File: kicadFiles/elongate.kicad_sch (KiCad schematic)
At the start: 137 parts, among them J1 TYPE-C-31-M12_13, SW1 MXSwitch, SW10 MXSwitch, SW11 MXSwitch, SW12 MXSwitch, SW13 MXSwitch, SW14 MXSwitch, SW15 MXSwitch, SW16 MXSwitch, SW17 MXSwitch, SW18 MXSwitch, SW19 MXSwitch, SW2 MXSwitch, SW20 MXSwitch, SW21 MXSwitch, SW22 MXSwitch, SW23 MXSwitch, SW24 MXSwitch, SW25 MXSwitch, SW26 MXSwitch, SW27 MXSwitch, SW28 MXSwitch, SW29 MXSwitch, SW3 MXSwitch, SW30 MXSwitch, SW31 MXSwitch, SW32 MXSwitch, SW33 MXSwitch, SW34 MXSwitch, SW35 MXSwitch, SW36 MXSwitch, SW37 MXSwitch, SW38 MXSwitch, SW39 MXSwitch, SW4 MXSwitch, SW40 MXSwitch, SW41 MXSwitch, SW42 MXSwitch, SW43 MXSwitch, SW44 MXSwitch, SW45 MXSwitch, SW46 MXSwitch, SW47 MXSwitch, SW48 MXSwitch, SW49 MXSwitch, SW5 MXSwitch, SW50 MXSwitch, SW51 MXSwitch, SW52 MXSwitch, SW53 MXSwitch, SW54 MXSwitch, SW6 MXSwitch, SW7 MXSwitch, SW8 MXSwitch, SW9 MXSwitch, U1 TPD4E05U06DQAR

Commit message: Change RCC resistors to R0402
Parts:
- R2, R3: footprint Resistor_SMD:R_0805_2012Metric_Pad1.15x1.40mm_HandSolder -> Resistor_SMD:R_0402_1005Metric; Package R1206 -> R0402

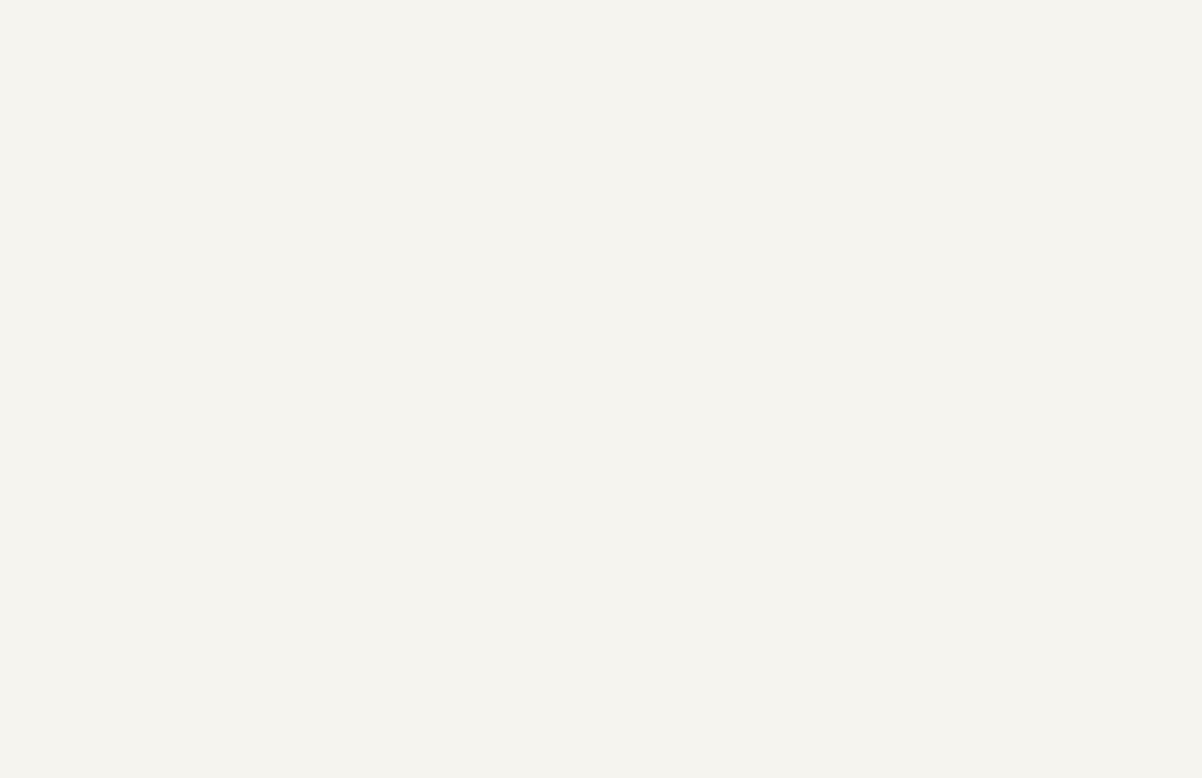
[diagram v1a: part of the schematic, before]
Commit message: Added LEDs
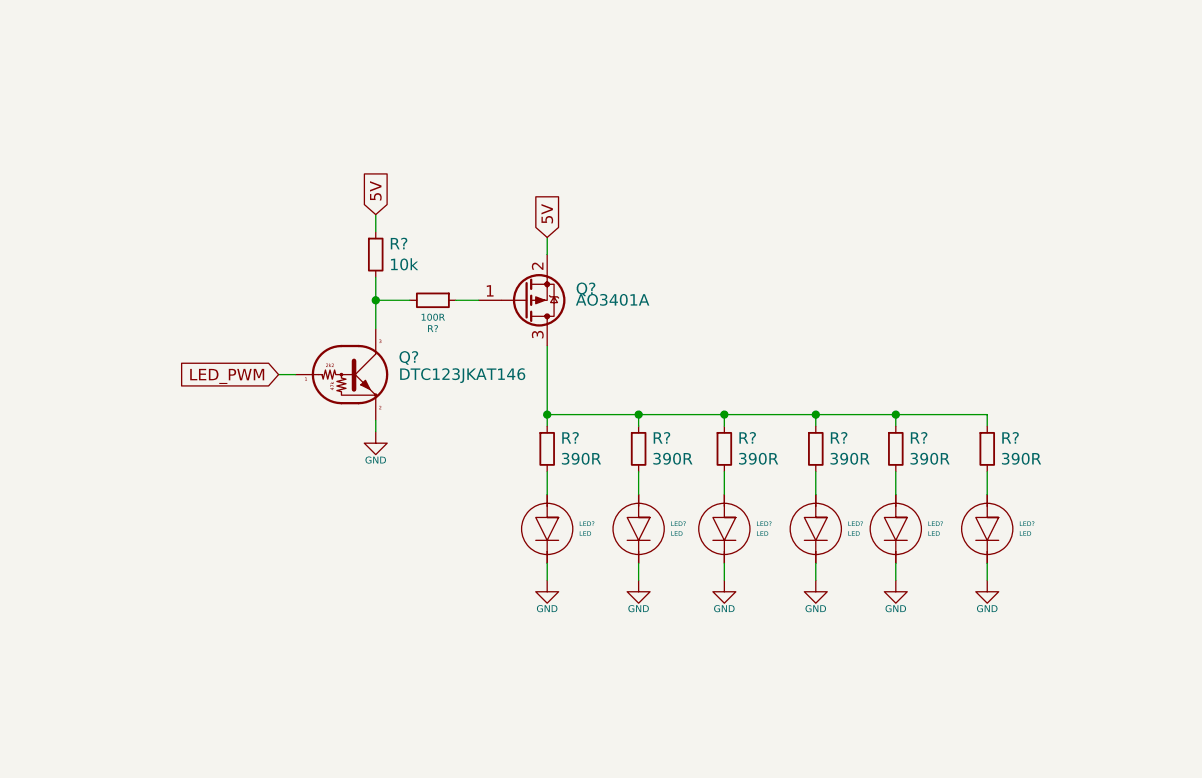
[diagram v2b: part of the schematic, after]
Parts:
- added LED? (x6): LED, acheron_Components:LED_THT_2.54mm, symbol acheronSymbols:LED
- added Q?: DTC123JKAT146, Package_TO_SOT_SMD:SOT-23, symbol acheronSymbols:DTC123J
- added Q?: AO3401A, Package_TO_SOT_SMD:SOT-23, symbol Transistor_FET:AO3401A
- added R? (x6): 390R, acheron_Components:R_SMD_1206, symbol Device:R_Small
- added R?: 100R, acheron_Components:R_SMD_1206, symbol Device:R_Small
- added R?: 10k, acheron_Components:R_SMD_1206, symbol Device:R_Small
- R10, R5, R6, R7, R8, R9: Package (none) -> R1206
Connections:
- net 5V: now also Q?.2 (S), R?.1
- net GND: now also LED?.K, LED?.K, LED?.K, LED?.K, LED?.K, LED?.K, Q?.2 (E)
- new net: Q?.3 (D), R?.1, R?.1, R?.1, R?.1, R?.1, R?.1
- new net: LED?.A, R?.2 (x6)
- new net: Q?.1 (G), R?.1
- new net: Q?.3 (C), R?.2, R?.2
- new net LED_PWM: Q?.1 (B)

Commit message: Finish LED placin, add MCU
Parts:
- added J2: AVR-JTAG-10, acheron_Connectors:Conn_ARM_JTAG_SWD_10, symbol Connector:AVR-JTAG-10
- added LED13, LED14, LED15, LED16, LED17, LED18, LED19, LED20, LED21, LED22, LED23, LED24, LED25, LED26, LED27, LED28, LED29, LED30, LED31, LED32, LED33, LED34, LED35, LED36, LED37, LED38, LED39, LED40, LED41, LED42, LED43, LED44, LED45, LED46, LED47, LED48, LED49, LED50, LED51, LED52, LED53, LED54, LED55, LED56, LED57, LED58, LED59, LED60: LED, acheron_Components:LED_THT_2.54mm, symbol acheronSymbols:LED
- added R20, R21, R22, R23, R24, R25, R26, R27, R28, R29, R30, R31, R32, R33, R34, R35, R36, R37, R38, R39, R40, R41, R42, R43, R44, R45, R46, R47, R48, R49, R50, R51, R52, R53, R54, R55, R56, R57, R58, R59, R60, R61, R62, R63, R64, R65, R66, R67: 390R, acheron_Components:R_SMD_1206, symbol Device:R_Small
- added U2: STM32F072CBT6, acheron_Components:LQFP-48_7x7mm_P0.5mm, symbol acheronSymbols:STM32F072-LQFP48
- gave numbers to parts that had none: 16
- renumbered C2 to C1, C1 to C2, D16 to D14, D17 to D15, D18 to D16, D19 to D17, D20 to D18, D21 to D19, D22 to D20, D23 to D21, D24 to D22, D25 to D23, D26 to D24, D27 to D25, D30 to D26, D31 to D27, D32 to D28, D33 to D29, D34 to D30, D35 to D31, D36 to D32, D37 to D33, D38 to D34, D39 to D35, D40 to D36, D41 to D37, D44 to D38, D45 to D39, D46 to D40, D47 to D41, D48 to D42, D49 to D43, D50 to D44, D51 to D45, D52 to D46, D42 to D47, D53 to D48, D15 to D49, D29 to D50, D43 to D51, D54 to D52, D14 to D53, D28 to D54, R2 to R1, R3 to R2, R4 to R3, R1 to R4, SW16 to SW14, SW17 to SW15, SW18 to SW16, SW19 to SW17, SW20 to SW18, SW21 to SW19, SW22 to SW20, SW23 to SW21, SW24 to SW22, SW25 to SW23, SW26 to SW24, SW27 to SW25, SW30 to SW26, SW31 to SW27, SW32 to SW28, SW33 to SW29, SW34 to SW30, SW35 to SW31, SW36 to SW32, SW37 to SW33, SW38 to SW34, SW39 to SW35, SW40 to SW36, SW41 to SW37, SW44 to SW38, SW45 to SW39, SW46 to SW40, SW47 to SW41, SW48 to SW42, SW49 to SW43, SW50 to SW44, SW51 to SW45, SW52 to SW46, SW42 to SW47, SW53 to SW48, SW15 to SW49, SW29 to SW50, SW43 to SW51, SW54 to SW52, SW14 to SW53, SW28 to SW54
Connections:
- net Col10: no longer SW53.1 (Col)
- net Col11: no longer SW54.1 (Col)
- net Col12: no longer SW47.1 (Col)
- net Col13: no longer SW48.1 (Col)
- net Col2: no longer SW49.1 (Col)
- net Col3: no longer SW50.1 (Col)
- net Col5: no longer SW51.1 (Col)
- net Col8: no longer SW52.1 (Col)
- net D+: now also U2.33 (USB_DP/PA12)
- net D-: now also U2.32 (USB_DM/TIM1_CH4/PA11)
- net GND: now also LED13.K, LED14.K, LED15.K, LED16.K, LED17.K, LED18.K, LED19.K, LED20.K, LED21.K, LED22.K, LED23.K, LED24.K, LED25.K, LED26.K, LED27.K, LED28.K, LED29.K, LED30.K, LED31.K, LED32.K, LED33.K, LED34.K, LED35.K, LED36.K, LED37.K, LED38.K, LED39.K, LED40.K, LED41.K, LED42.K, LED43.K, LED44.K, LED45.K, LED46.K, LED47.K, LED48.K, LED49.K, LED50.K, LED51.K, LED52.K, LED53.K, LED54.K, LED55.K, LED56.K, LED57.K, LED58.K, LED59.K, LED60.K
- net LED_PWM: now also U2.16 (PA6/ADC_IN6/TIM3_CH1/TIM16_CH1)
- net Row1: now also D49.1 (K), D53.1 (K)
- net Row2: now also D50.1 (K), D54.1 (K)
- net Row3: now also D47.1 (K), D51.1 (K)
- net Row4: now also D48.1 (K), D52.1 (K)
- net at Q1.3 (D), R14.1, R15.1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: now also R20.1, R21.1, R22.1, R23.1, R24.1, R25.1, R26.1, R27.1, R28.1, R29.1, R30.1, R31.1, R32.1, R33.1, R34.1, R35.1, R36.1, R37.1, R38.1, R39.1, R40.1, R41.1, R42.1, R43.1, R44.1, R45.1, R46.1, R47.1, R48.1, R49.1, R50.1, R51.1, R52.1, R53.1, R54.1, R55.1, R56.1, R57.1, R58.1, R59.1, R60.1, R61.1, R62.1, R63.1, R64.1, R65.1, R66.1, R67.1
- removed net Row5: D47.1 (K), D48.1 (K), D49.1 (K), D50.1 (K), D51.1 (K), D52.1 (K), D53.1 (K), D54.1 (K)
- new net: LED50.A, R57.2
- new net: LED47.A, R54.2
- new net: LED24.A, R31.2
- new net: LED60.A, R67.2
- new net: LED57.A, R64.2
- new net: LED30.A, R37.2
- new net: LED41.A, R48.2
- new net: LED32.A, R39.2
- new net: LED14.A, R21.2
- new net: LED36.A, R43.2
- new net: LED35.A, R42.2
- new net: LED23.A, R30.2
- new net: LED31.A, R38.2
- new net: LED48.A, R55.2
- new net: LED53.A, R60.2
- new net: LED56.A, R63.2
- new net: LED25.A, R32.2
- new net: LED45.A, R52.2
- new net: LED51.A, R58.2
- new net: LED44.A, R51.2
- new net: LED17.A, R24.2
- new net: LED16.A, R23.2
- new net: LED34.A, R41.2
- new net: LED18.A, R25.2
- new net: LED21.A, R28.2
- new net: LED39.A, R46.2
- new net: LED46.A, R53.2
- new net: LED19.A, R26.2
- new net: LED42.A, R49.2
- new net: LED29.A, R36.2
- new net: J2.10 (GND), J2.2 (GND)
- new net: LED26.A, R33.2
- new net: LED33.A, R40.2
- new net: LED49.A, R56.2
- new net: LED15.A, R22.2
- new net: LED22.A, R29.2
- new net: LED55.A, R62.2
- new net: LED20.A, R27.2
- new net: LED58.A, R65.2
- new net: LED37.A, R44.2
- new net: LED38.A, R45.2
- new net: LED59.A, R66.2
- new net: LED54.A, R61.2
- new net: LED52.A, R59.2
- new net: LED43.A, R50.2
- new net: LED27.A, R34.2
- new net: LED13.A, R20.2
- new net: LED28.A, R35.2
- new net: LED40.A, R47.2
- new net Col14: SW47.1 (Col), SW48.1 (Col), SW53.1 (Col), SW54.1 (Col)
- new net Col15: SW49.1 (Col), SW50.1 (Col), SW51.1 (Col), SW52.1 (Col)
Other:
- moved on the sheet: C3, D47, D48, D49, D50, D51, D52, D53, D54, D55, F1, LED10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

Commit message: Almost finish routing, DRC pending
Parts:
- removed J2: AVR-JTAG-10, acheron_Connectors:Conn_ARM_JTAG_SWD_10, symbol Connector:AVR-JTAG-10
- added C10, C11, C12, C13, C14, C15, C16, C17, C18, C19, C4, C5, C6, C7, C8, C9: 1u, Capacitor_SMD:C_0805_2012Metric_Pad1.15x1.40mm_HandSolder, symbol Device:C_Small
- added C20: 100u, Capacitor_SMD:C_0805_2012Metric_Pad1.15x1.40mm_HandSolder, symbol Device:C_Small
- added C21: 10u, Capacitor_SMD:C_0805_2012Metric_Pad1.15x1.40mm_HandSolder, symbol Device:C_Small
- added D56, D57, D58, D59, D60, D61, D62, D63, D64, D65, D66, D67, D68, D69, D70, D71: WS2812C, acheron_Components:LED_WS2812B_5.0x5.0mm_P3.2mm, symbol LED:WS2812B
- added D72: 1N4148, acheron_Components:D_SOD-123, symbol Device:D
- added J2: Conn_ARM_JTAG_SWD_10, acheron_Connectors:Conn_ARM_JTAG_SWD_10, symbol Connector:Conn_ARM_JTAG_SWD_10
- added J3: Conn_01x11, acheron_Connectors:PinHeader_2x5_P2.54mm_Vertical, symbol Connector_Generic:Conn_01x11
- added Q3: AO3401A, Package_TO_SOT_SMD:SOT-23, symbol Transistor_FET:AO3401A
- added Q4: DTC123JKAT146, Package_TO_SOT_SMD:SOT-23, symbol acheronSymbols:DTC123J
- added R68, R69, R70, R71, R72, R73, R74, R75, R76, R77, R78, R79, R80, R81, R82, R83: 3R, acheron_Components:R_SMD_1206, symbol Device:R_Small
- added R84, R86: 10k, acheron_Components:R_SMD_1206, symbol Device:R_Small
- added R85: 5.1k, acheron_Components:R_SMD_1206, symbol Device:R_Small
- added R87: 100k, acheron_Components:R_SMD_1206, symbol Device:R_Small
- added R88: 100R, acheron_Components:R_SMD_1206, symbol Device:R_Small
- added R89: 33k, acheron_Components:R_SMD_1206, symbol Device:R_Small
- added SW55: SW_Push, acheron_Hardware:smdPushBtn, symbol Switch:SW_Push
- D1, D10, D11, D12, D13, D2, D3, D4, D5, D6, D7, D8, D9: Package (none) -> SOD-123
- D14: renamed from D53; Package (none) -> SOD-123
- D15: renamed from D49; Package (none) -> SOD-123
- D16: renamed from D14; Package (none) -> SOD-123
- D17: renamed from D15; Package (none) -> SOD-123
- D18: renamed from D16; Package (none) -> SOD-123
- D19: renamed from D17; Package (none) -> SOD-123
- D20: renamed from D18; Package (none) -> SOD-123
- D21: renamed from D19; Package (none) -> SOD-123
- D22: renamed from D20; Package (none) -> SOD-123
- D23: renamed from D21; Package (none) -> SOD-123
- D24: renamed from D22; Package (none) -> SOD-123
- D25: renamed from D23; Package (none) -> SOD-123
- D26: renamed from D24; Package (none) -> SOD-123
- D27: renamed from D25; Package (none) -> SOD-123
- D28: renamed from D54; Package (none) -> SOD-123
- D29: renamed from D50; Package (none) -> SOD-123
- D30: renamed from D26; Package (none) -> SOD-123
- D31: renamed from D27; Package (none) -> SOD-123
- D32: renamed from D28; Package (none) -> SOD-123
- D33: renamed from D29; Package (none) -> SOD-123
- D34: renamed from D30; Package (none) -> SOD-123
- D35: renamed from D31; Package (none) -> SOD-123
- D36: renamed from D32; Package (none) -> SOD-123
- D37: renamed from D33; Package (none) -> SOD-123
- D38: renamed from D34; Package (none) -> SOD-123
- D39: renamed from D35; Package (none) -> SOD-123
- D40: renamed from D36; Package (none) -> SOD-123
- D41: renamed from D37; Package (none) -> SOD-123
- D42: renamed from D47; Package (none) -> SOD-123
- D43: renamed from D51; Package (none) -> SOD-123
- D44: renamed from D38; Package (none) -> SOD-123
- D45: renamed from D39; Package (none) -> SOD-123
- D46: renamed from D40; Package (none) -> SOD-123
- D47: renamed from D41; Package (none) -> SOD-123
- D48: renamed from D42; Package (none) -> SOD-123
- D49: renamed from D43; Package (none) -> SOD-123
- D50: renamed from D44; Package (none) -> SOD-123
- D51: renamed from D45; Package (none) -> SOD-123
- D52: renamed from D46; Package (none) -> SOD-123
- D53: renamed from D48; Package (none) -> SOD-123
- D54: renamed from D52; Package (none) -> SOD-123
- renumbered SW53 to SW14, SW49 to SW15, SW14 to SW16, SW15 to SW17, SW16 to SW18, SW17 to SW19, SW18 to SW20, SW19 to SW21, SW20 to SW22, SW21 to SW23, SW22 to SW24, SW23 to SW25, SW24 to SW26, SW25 to SW27, SW54 to SW28, SW50 to SW29, SW26 to SW30, SW27 to SW31, SW28 to SW32, SW29 to SW33, SW30 to SW34, SW31 to SW35, SW32 to SW36, SW33 to SW37, SW34 to SW38, SW35 to SW39, SW36 to SW40, SW37 to SW41, SW47 to SW42, SW51 to SW43, SW38 to SW44, SW39 to SW45, SW40 to SW46, SW41 to SW47, SW42 to SW48, SW43 to SW49, SW44 to SW50, SW45 to SW51, SW46 to SW52, SW48 to SW53, SW52 to SW54
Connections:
- net 5V: now also R68.1, R69.1, R70.1, R71.1, R72.1, R73.1, R74.1, R75.1, R76.1, R77.1, R78.1, R79.1, R80.1, R81.1, R82.1, R83.1, R84.1, R85.1
- net GND: now also U2.23 (VSS), U2.35 (VSS), U2.8 (VSSA), C10.2, C11.2, C12.2, C13.2, C14.2, C15.2, C16.2, C17.2, C18.2, C19.2, C20.1, C21.1, C4.2, C5.2, C6.2, C7.2, C8.2, C9.2, D56.3 (VSS), D57.3 (VSS), D58.3 (VSS), D59.3 (VSS), D60.3 (VSS), D61.3 (VSS), D62.3 (VSS), D63.3 (VSS), D64.3 (VSS), D65.3 (VSS), D66.3 (VSS), D67.3 (VSS), D68.3 (VSS), D69.3 (VSS), D70.3 (VSS), D71.3 (VSS), J2.3 (GND), J2.5 (GND), J2.9 (GNDDetect), Q4.2 (E), R86.2, R87.2
- net 3V3: now reaches U2.1 (VBAT)
- net 3V3: now also U2.24 (VDD), U2.36 (VDDIO2), U2.48 (VDD), U2.9 (VDDA)
- net RGB_3V3: now reaches U2.28 (SPI2_MOSI/I2S2_SD/PB15)
- net RGB_3V3: now also Q3.3 (D)
- net SWDIO: now reaches U2.34 (SWDIO/PA13)
- net SWDIO: now also J2.2 (SWDIO/TMS)
- net SWCLK: now reaches U2.37 (SWCLK/PA14)
- net SWCLK: now also J2.4 (SWDCLK/TCK)
- net BOOT0: now reaches U2.44 (BOOT0)
- net BOOT0: now also C20.2, R87.1, R89.1
- net nRST: now reaches U2.7 (NRST)
- net nRST: now also C21.2, J2.10 (~RESET~), R88.1
- new net: D72.2 (A), Q4.1 (B), SW55.2
- new net: C5.1, D57.1 (VDD), R69.2
- new net: C19.1, D71.1 (VDD), R83.2
- new net: D70.2 (DOUT), D71.4 (DIN)
- new net: C15.1, D67.1 (VDD), R79.2
- new net: D67.2 (DOUT), D68.4 (DIN)
- new net: D66.2 (DOUT), D67.4 (DIN)
- new net: C16.1, D68.1 (VDD), R80.2
- new net: D68.2 (DOUT), D69.4 (DIN)
- new net: D72.1 (K), R89.2
- new net: Q4.3 (C), R88.2
- new net: C6.1, D58.1 (VDD), R70.2
- new net: D58.2 (DOUT), D59.4 (DIN)
- new net: D57.2 (DOUT), D58.4 (DIN)
- new net: C18.1, D70.1 (VDD), R82.2
- new net: C8.1, D60.1 (VDD), R72.2
- new net: Q3.1 (G), R85.2, R86.1
- new net: C17.1, D69.1 (VDD), R81.2
- new net: C10.1, D62.1 (VDD), R74.2
- new net: D62.2 (DOUT), D63.4 (DIN)
- new net: D61.2 (DOUT), D62.4 (DIN)
- new net: D69.2 (DOUT), D70.4 (DIN)
- new net: C7.1, D59.1 (VDD), R71.2
- new net: D60.2 (DOUT), D61.4 (DIN)
- new net: D59.2 (DOUT), D60.4 (DIN)
- new net: C4.1, D56.1 (VDD), R68.2
- new net: C14.1, D66.1 (VDD), R78.2
- new net: C13.1, D65.1 (VDD), R77.2
- new net: C11.1, D63.1 (VDD), R75.2
- new net: D63.2 (DOUT), D64.4 (DIN)
- new net: C12.1, D64.1 (VDD), R76.2
- new net: D64.2 (DOUT), D65.4 (DIN)
- new net: C9.1, D61.1 (VDD), R73.2
- new net: D56.2 (DOUT), D57.4 (DIN)
- new net: D65.2 (DOUT), D66.4 (DIN)
- new net 3.3V: SW55.1
- new net RGB_5V: D56.4 (DIN), Q3.2 (S), R84.2
- no-connect marks 2 -> 5
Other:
- moved on the sheet: U2

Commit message: Finish routing
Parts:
- added C10, C4, C5, C6: 100n, Capacitor_SMD:C_0402_1005Metric, symbol Device:C_Small
- added C11, C7: 4.7u, Capacitor_SMD:C_0402_1005Metric, symbol Device:C_Small
- added C30: 1u, Capacitor_SMD:C_0805_2012Metric_Pad1.15x1.40mm_HandSolder, symbol Device:C_Small
- added C8: 1u, Capacitor_SMD:C_0402_1005Metric, symbol Device:C_Small
- added C9: 10n, Capacitor_SMD:C_0402_1005Metric, symbol Device:C_Small
- added D73: RB060M-60TR, acheron_Components:D_SOD-123, symbol Device:D_Schottky
- added R90: 100k, acheron_Components:R_SMD_1206, symbol Device:R_Small
- added U3: MCP1700-3302E, Package_TO_SOT_SMD:SOT-23, symbol Regulator_Linear:MCP1700-3302E_SOT23
- F1: value Polyfuse -> RF1338-000; LCSC Part Number (none) -> C207188; Manufacturer (none) -> Littelfuse; Manufacturer Part Number (none) -> RF1338-000
- J3: value Conn_01x11 -> Conn_01x10; symbol Connector_Generic:Conn_01x11 -> Connector_Generic:Conn_01x10
- R11: value 1M -> 100k
- SW55: value SW_Push -> K2-1187SQ-A4SW-06; LCSC Part Number (none) -> C92584; Manufacturer (none) -> Korean Hroparts Elec; Manufacturer Part Number (none) -> K2-1187SQ-A4SW-06; Package (none) -> 5.1x5.1mm
- renumbered C4 to C12, C5 to C13, C6 to C14, C7 to C15, C8 to C16, C9 to C17, C10 to C18, C11 to C19, C12 to C20, C13 to C21, C14 to C22, C15 to C23, C16 to C24, C17 to C25, C18 to C26, C19 to C27, C20 to C28, C21 to C29, D44 to D40, D45 to D41, D46 to D42, D47 to D43, D48 to D44, D49 to D45, D50 to D46, D51 to D47, D52 to D48, D53 to D49, D54 to D50, D40 to D51, D41 to D52, D42 to D53, D43 to D54, R89 to R87, R87 to R88, R88 to R89, SW44 to SW40, SW45 to SW41, SW46 to SW42, SW47 to SW43, SW48 to SW44, SW49 to SW45, SW50 to SW46, SW51 to SW47, SW52 to SW48, SW53 to SW49, SW54 to SW50, SW40 to SW51, SW41 to SW52, SW42 to SW53, SW43 to SW54
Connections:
- net 3.3V is gone; now on net 3V3: SW55.1
- net 3V3: now also J2.1 (VTref), C10.1, C11.1, C30.2, C4.2, C5.1, C6.1, C7.1, C8.2, C9.2, D73.2 (A), R90.1, U3.2 (VO)
- net 5V: now also D73.1 (K), U3.3 (VI)
- net Col1: now also U2.31 (TIM1_CH3/PA10)
- net Col10: now also U2.17 (PA7/TIM3_CH2/TIM14_CH1/ADC_IN7)
- net Col11: now also U2.15 (PA5/ADC_IN5/DAC_OUT2)
- net Col12: now also U2.46 (SPI2_NSS/I2S2_WS/I2C1_SDA/TIM17_CH1/PB9)
- net Col13: now also U2.45 (I2C1_SCL/TIM16_CH1/PB8)
- net Col14: now also U2.43 (2C1_SDA/PB7)
- net Col15: now also U2.42 (I2C1_SCL/PB6)
- net Col2: now also U2.30 (TIM1_CH2/PA9)
- net Col3: now also U2.29 (TIM1_CH1/PA8)
- net Col4: now also U2.27 (PB14/SPI2_MISO/I2S2_MCK/I2C2_SDA/TIM15_CH1/PB15)
- net Col5: now also U2.25 (PB12)
- net Col6: now also U2.22 (PB11/TIM2_CH4/I2C2_SDA)
- net Col7: now also U2.21 (PB10/SPI2_SCK/I2C2_SCL/TIM2_CH3)
- net Col8: now also U2.20 (PB2)
- net Col9: now also U2.19 (PB1/TIM3_CH4/TIM14_CH1/ADC_IN9)
- net GND: now also U2.47 (VSS), C10.2, C11.2, C30.1, C4.1, C5.2, C6.2, C7.2, C8.1, C9.1, R90.2, U3.1 (GND)
- net Row1: now also U2.39 (SPI1_SCK/I2S1_CK/TIM2_CH2/PB3)
- net Row2: now also U2.38 (PA2)
- net Row3: now also U2.18 (PB0/TIM3_CH3/ADC_IN8); no longer D51.1 (K), D52.1 (K), D53.1 (K), D54.1 (K)
- net Row4: now also U2.40 (SPI1_MISO/I2S1_MCK/TIM3_CH1/PB4)
- net EXTRA_6: now reaches U2.10 (PA0/ADC_IN0)
- net EXTRA_6: now also J3.6 (Pin_6)
- net EXTRA_7: now reaches U2.11 (PA1/ADC_IN1)
- net EXTRA_7: now also J3.7 (Pin_7)
- net EXTRA_8: now reaches U2.12 (PA2/ADC_IN2)
- net EXTRA_8: now also J3.8 (Pin_8)
- net EXTRA_9: now reaches U2.13 (PA3/TIM15_CH2/ADC_IN3)
- net EXTRA_9: now also J3.9 (Pin_9)
- net EXTRA_10: now reaches U2.14 (PA4/TIM14_CH1/ADC_IN4)
- net EXTRA_10: now also J3.10 (Pin_10)
- net EXTRA_1: now reaches U2.2 (PC13)
- net EXTRA_1: now also J3.1 (Pin_1)
- net EXTRA_2: now reaches U2.3 (PC14/OSC32_IN)
- net EXTRA_2: now also J3.2 (Pin_2)
- net EXTRA_3: now reaches U2.4 (PC15/OSC32_OUT)
- net EXTRA_3: now also J3.3 (Pin_3)
- net Row5: now reaches U2.41 (SPI1_MOSI/I2S1_SD/TIM3_CH2/PB5)
- net Row5: now also D51.1 (K), D52.1 (K), D53.1 (K), D54.1 (K)
- net EXTRA_4: now reaches U2.5 (PF0/OSC_IN)
- net EXTRA_4: now also J3.4 (Pin_4)
- net EXTRA_5: now reaches U2.6 (PF1/OSC_OUT)
- net EXTRA_5: now also J3.5 (Pin_5)
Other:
- moved on the sheet: D51, D52, D53, D54, SW51, SW52, SW53, SW54

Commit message: DRC ran, added indicators
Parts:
- J3: value Conn_01x10 -> Conn_01x6; footprint acheron_Connectors:PinHeader_2x5_P2.54mm_Vertical -> acheron_Connectors:PinHeader_2x3_P2.54mm_Vertical; symbol Connector_Generic:Conn_01x10 -> Connector_Generic:Conn_01x06
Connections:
- net 3V3: now also J3.5 (Pin_5)
- net GND: now also J3.6 (Pin_6)
- net INDICATOR1: now also U2.12 (PA2/ADC_IN2)
- net INDICATOR2: now also U2.11 (PA1/ADC_IN1)
- net INDICATOR3: now also U2.10 (PA0/ADC_IN0)
- net INDICATOR4: now also U2.14 (PA4/TIM14_CH1/ADC_IN4)
- net INDICATOR5: now also U2.13 (PA3/TIM15_CH2/ADC_IN3)
- net INDICATOR6: now also U2.6 (PF1/OSC_OUT)
- removed net EXTRA_10: J3.10 (Pin_10), U2.14 (PA4/TIM14_CH1/ADC_IN4)
- removed net EXTRA_5: J3.5 (Pin_5), U2.6 (PF1/OSC_OUT)
- removed net EXTRA_6: J3.6 (Pin_6), U2.10 (PA0/ADC_IN0)
- removed net EXTRA_7: J3.7 (Pin_7), U2.11 (PA1/ADC_IN1)
- removed net EXTRA_8: J3.8 (Pin_8), U2.12 (PA2/ADC_IN2)
- removed net EXTRA_9: J3.9 (Pin_9), U2.13 (PA3/TIM15_CH2/ADC_IN3)
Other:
- note added: "JTAG SWD"
- note added: "LDO"
- note added: "LEDs"
- note added: "MCU Reset"
- note removed: "REFERENCES"
- note removed: "[1] ATMEGA32U4 datasheet"
- note removed: "[2] AN2519 Application Note: AVR® Microcontroller Hardware Design Considerations"
- note removed: "[3] NX5032GC 16MHz crystal datasheet"
- note removed: "[4] AN232B-06 Application Note"
- note removed: "[5] USBLC6-2 Datasheet"
- note removed: "http://ww1.microchip.com/downloads/en/AppNotes/AN2519-AVR-Microcontroller-Hardware-Design-Considerations-00002519B.pdf"
- note removed: "http://ww1.microchip.com/downloads/en/DeviceDoc/Atmel-7766-8-bit-AVR-ATmega16U4-32U4_Datasheet.pdf"
- note removed: "https://www.ftdichip.com/Support/Documents/AppNotes/AN232B-06_11.pdf"
- note removed: "https://www.ndk.com/images/products/catalog/c_NX5032GC-STD-CSK-6_e.pdf"
- note removed: "https://www.st.com/resource/en/datasheet/usblc6-2.pdf"
- moved on the sheet: C10, C11, C12, C13, C14, C15, C16, C17, C18, C19, C20, C21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

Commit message: Solve symbol fields issues, prepare for pre-release Gamma
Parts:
- D73: LCSC Part No. C114257 -> (none); LCSC Part Number (none) -> C114257; Manufacturer Part No. RB060M-60TR -> (none); Manufacturer Part Number (none) -> RB060M-60TR
- J1: Manufacturer Part Number (none) -> TYPE-C-31-M-12; Manufacturer Product Number TYPE-C-31-M-12 -> (none)
- J2, J3, L1, L2, L3, L4, L5, SW1, SW10, SW11, SW12, SW13, SW14, SW15, SW16, SW17, SW18, SW19, SW2, SW20, SW21, SW22, SW23, SW24, SW25, SW26, SW27, SW28, SW29, SW3, SW30, SW31, SW32, SW33, SW34, SW35, SW36, SW37, SW38, SW39, SW4, SW40, SW41, SW42, SW43, SW44, SW45, SW46, SW47, SW48, SW49, SW5, SW50, SW51, SW52, SW53, SW54, SW6, SW7, SW8, SW9: now left out of the parts list
- U2: Manufacturer (none) -> STMicroelectronics; Mnanufacturer STMicroelectronics -> (none)
- U3: LCSC Part No. C39051 -> (none); LCSC Part Number (none) -> C39051; Manufacturer Part No. MCP1700-3302E/TT -> (none); Manufacturer Part Number (none) -> MCP1700-3302E/TT

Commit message: Solved level translator circuit issues
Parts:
- removed Q3: AO3401A, Package_TO_SOT_SMD:SOT-23, symbol Transistor_FET:AO3401A
- added C31: 1u, Capacitor_SMD:C_0805_2012Metric, symbol Device:C_Small
- added Q3: AO3400A, Package_TO_SOT_SMD:SOT-23, symbol Transistor_FET:AO3400A
- D55: value SMF9.0CA -> SMF6.0A; footprint acheron_Components:D_SOD-123_Bidirectional -> acheron_Components:D_SOD-123; symbol Device:D_TVS -> Device:D_Schottky; LCSC Part Number C435473 -> C435458; Manufacturer Part Number SMF9.0CA -> SMF6.0A; Package SOD-123B -> SOD-123
- R10, R14, R15, R16, R17, R18, R19, R20, R21, R22, R23, R24, R25, R26, R27, R28, R29, R30, R31, R32, R33, R34, R35, R36, R37, R38, R39, R40, R41, R42, R43, R44, R45, R46, R47, R48, R49, R5, R50, R51, R52, R53, R54, R55, R56, R57, R58, R59, R6, R60, R61, R62, R63, R64, R65, R66, R67, R7, R8, R9: value 390R -> 470R
- U2: Manufacturer Part Number STM32F072CBT6 -> (none)
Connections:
- net 5V: now also D55.1 (K); no longer D55.2 (A2)
- net GND: now also D55.2 (A), C31.1; no longer D55.1 (A1)
- net RGB_3V3: now also Q3.2 (S)
- net RGB_5V: now also Q3.3 (D)
- net at R85.2, R86.1: now also C31.2, Q3.1 (G)
